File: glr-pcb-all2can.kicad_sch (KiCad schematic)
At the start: 43 parts, among them IC2 ZMR330FTA, IC4 STM32C092KCT6, IC5 AP64060WU-7, IC6 AP64060WU-7, J1 Conn_02x02_Counter_Clockwise_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, J2 Conn_02x02_Counter_Clockwise_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, J3 Conn_02x02_Counter_Clockwise_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, J4 Conn_02x02_Counter_Clockwise_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, J5 Conn_01x04, J6 Conn_01x02, J7 Conn_01x02, J8 62701021621

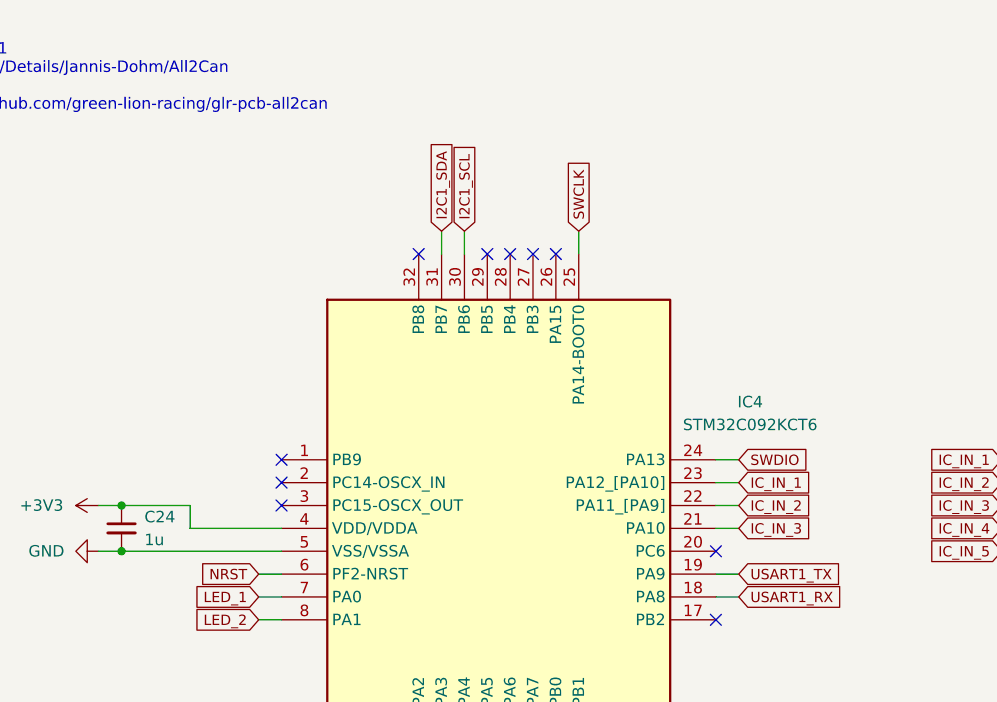
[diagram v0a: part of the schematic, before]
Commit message: routing mostly done
* missed that there need to be holes in bopla housing
* add stm32 chip datasheet
* remove unused würth library
* change pins on chip of sensor data input
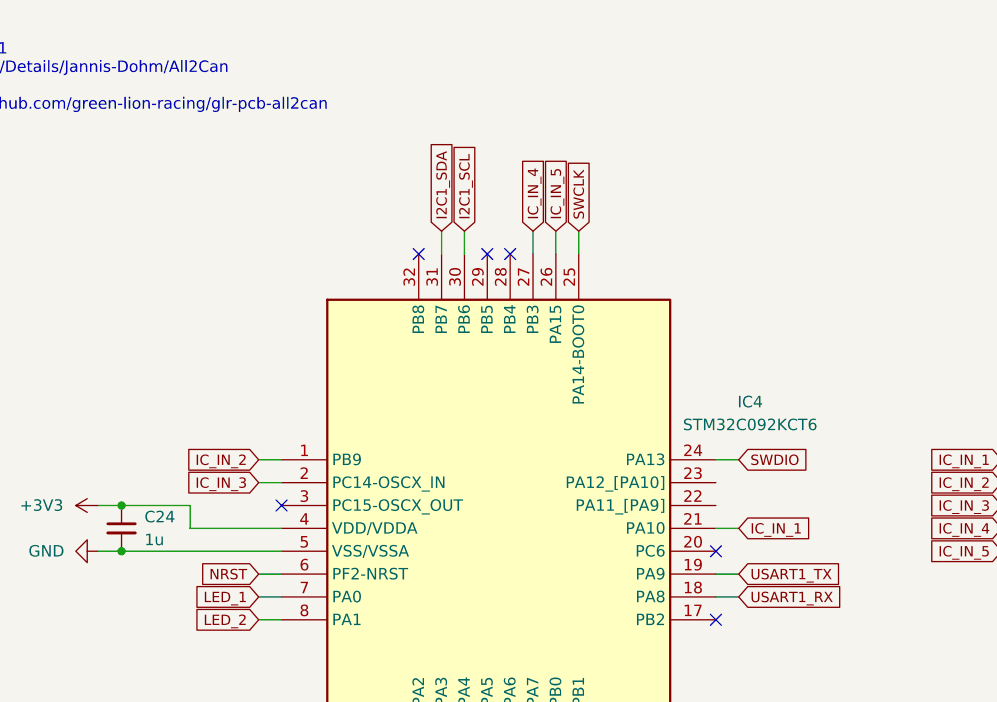
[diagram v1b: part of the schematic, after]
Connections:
- net IC_IN_1: now also IC4.21 (PA10); no longer IC4.23 (PA12_[PA10])
- net IC_IN_2: now also IC4.1 (PB9); no longer IC4.22 (PA11_[PA9])
- net IC_IN_3: now also IC4.2 (PC14-OSCX_IN); no longer IC4.21 (PA10)
- net IC_IN_4: now also IC4.27 (PB3)
- net IC_IN_5: now also IC4.26 (PA15)
- no-connect marks 16 -> 12

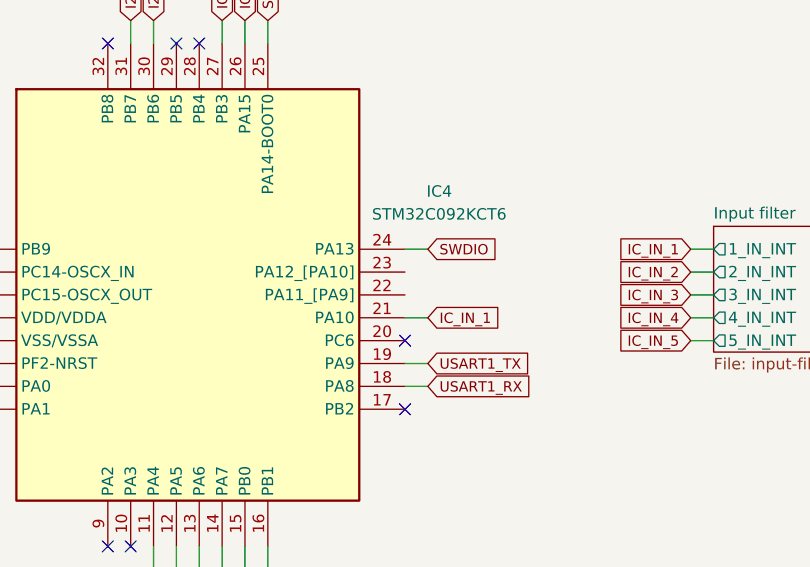
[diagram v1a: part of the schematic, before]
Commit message: update to merged glr kicad library
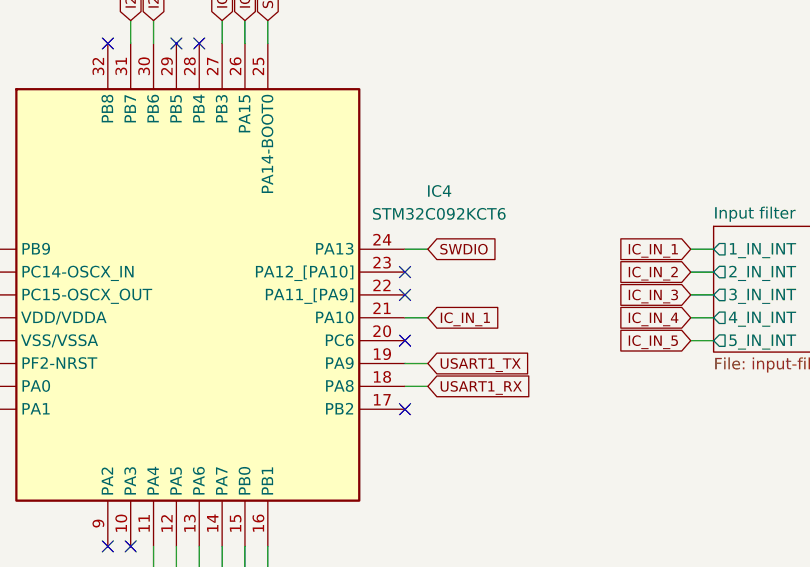
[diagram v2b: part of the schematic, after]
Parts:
- IC5, IC6: footprint SOT95P280X100-6N -> SamacSys_Parts:SOT95P280X100-6N
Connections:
- no-connect marks 12 -> 14
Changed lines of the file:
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@@
 	)
 	(no_connect
+		(at 172.72 68.58)
+	)
+	(no_connect
 		(at 172.72 81.28)
 	)
 	(no_connect
+		(at 172.72 66.04)
+	)
+	(no_connect
 		(at 124.46 68.58)
 	)
@@
 			)
 		)
-		(property "Footprint" "SOT95P280X100-6N"
+		(property "Footprint" "SamacSys_Parts:SOT95P280X100-6N"
 			(at 74.93 225.73 0)
 			(hide yes)
@@
 			)
 		)
-		(property "Footprint" "SOT95P280X100-6N"
+		(property "Footprint" "SamacSys_Parts:SOT95P280X100-6N"
 			(at 74.93 266.37 0)
 			(hide yes)
